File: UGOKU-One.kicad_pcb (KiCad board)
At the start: 2 copper layers, 63 x 63 mm, 57 parts, among them J1 PB0, J2 PA10, J3 Conn_01x02_Male, J4 PA10, J6 Conn_01x04, SW1 PF1, SW2 RESET, SW3 SW_Push_DPDT, SW5 SW_Push_DPDT, T3 PTS_1.5_2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

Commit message: 2024/1/6発注仕様
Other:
- board text added: "UGOKU One Ver0.43 UGOKU Lab 2024-1"
- board text added: "https://github.com/UGOKU-Lab/UGOKU-One"
- board text removed: "UGOKU One Ver0.43 UGOKU-Lab 2024-1"
- board text removed: "https://github.com/UGOKU-Lab/MultiBoardMini_HW"

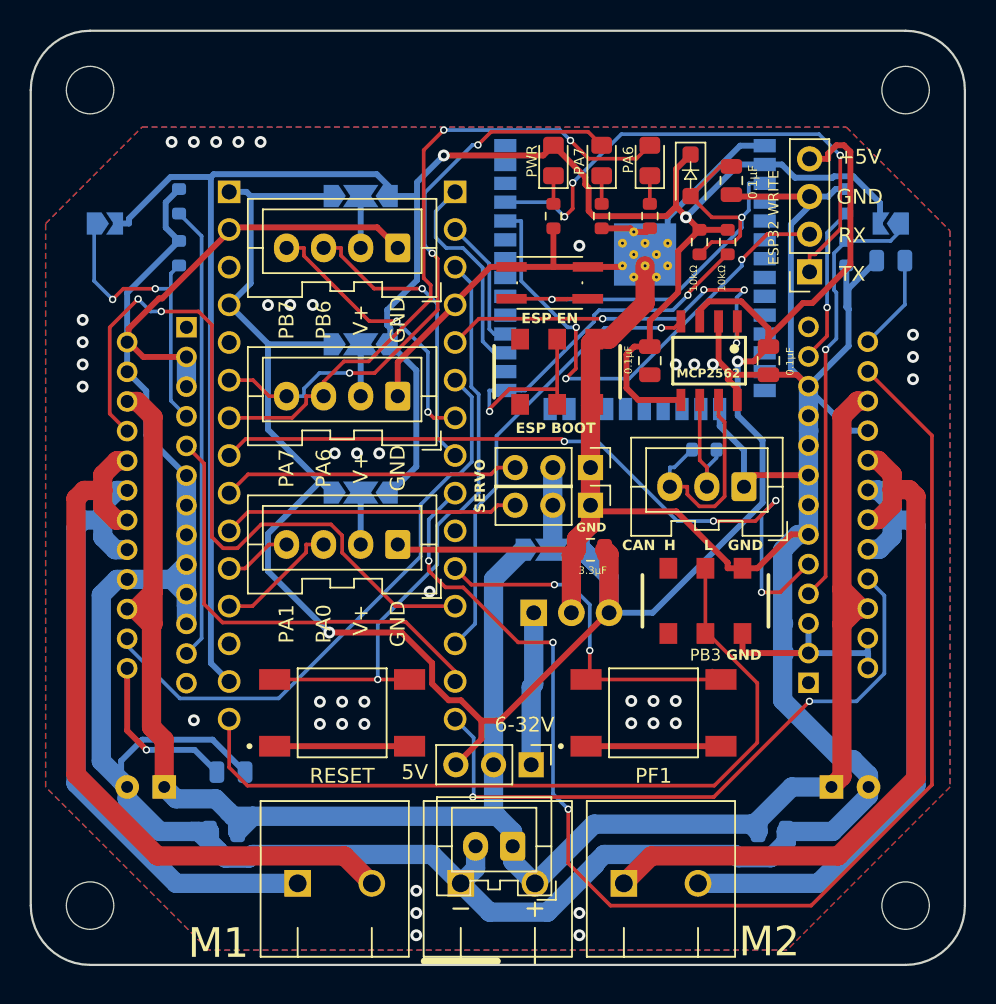
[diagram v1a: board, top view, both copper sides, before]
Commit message: Via size modified to match JLCPCB rules
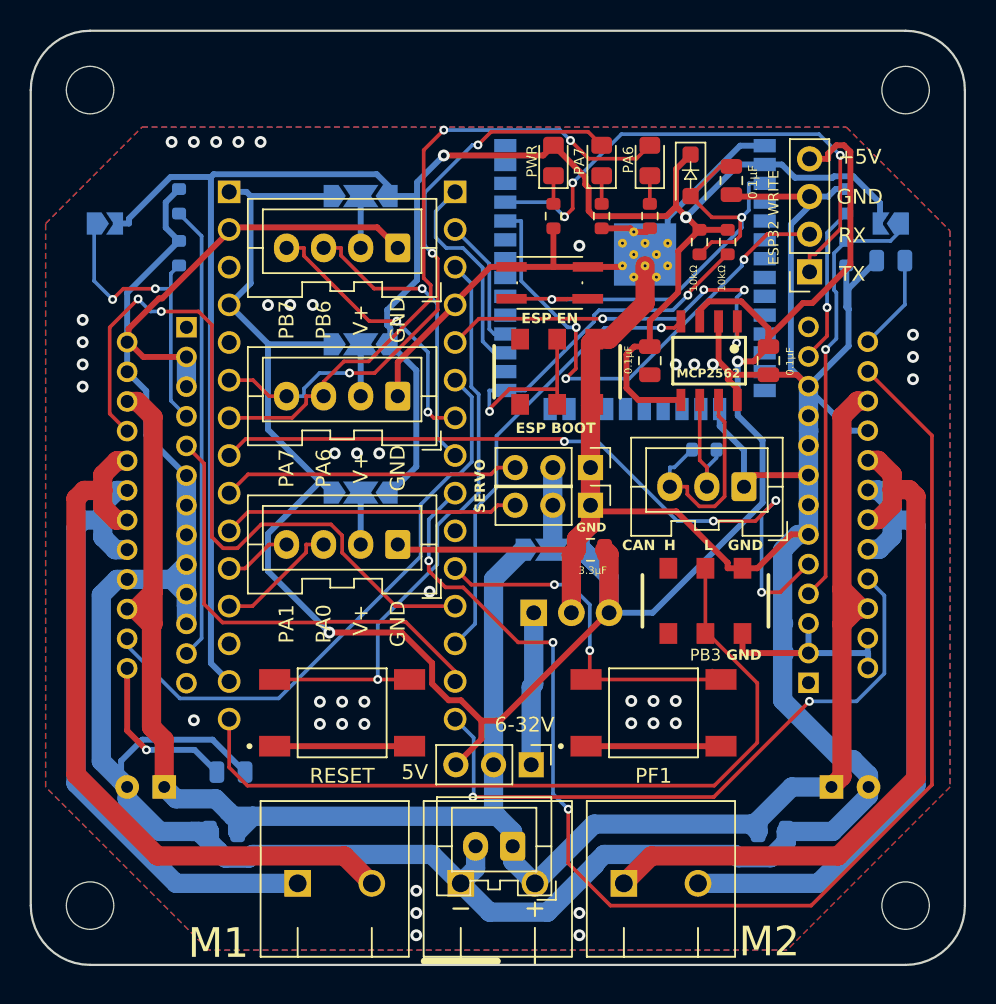
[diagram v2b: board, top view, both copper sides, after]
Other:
- board text added: "UGOKU One Ver0.4.4 UGOKU Lab 2024-1"
- board text removed: "UGOKU One Ver0.43 UGOKU Lab 2024-1"

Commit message: Motor driver STM pin assignment replacement
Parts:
- renumbered MOTOR2 to MOTOR_A1, MOTOR1 to MOTOR_B1
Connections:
- U4 pad 9: Net-(U2B-PA5) -> Net-(U2A-PB5)
- U5 pad 8: Net-(U2A-PA8) -> Net-(U2B-PA5)
- U5 pad 9: Net-(U2A-PB5) -> Net-(U2A-PA8)
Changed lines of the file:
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@@
     (property "Sheetname" "")
     (attr through_hole)
-    (fp_text reference "MOTOR1" (at 0 0) (layer "F.SilkS") hide
+    (fp_text reference "MOTOR_B1" (at 0 0) (layer "F.SilkS") hide
         (effects (font (size 1.27 1.27) (thickness 0.15)) (justify right top))
     )
@@
     (property "Sheetname" "")
     (attr through_hole)
-    (fp_text reference "MOTOR2" (at 0 0) (layer "F.SilkS") hide
+    (fp_text reference "MOTOR_A1" (at 0 0) (layer "F.SilkS") hide
         (effects (font (size 1.27 1.27) (thickness 0.15)) (justify right top))
     )
@@
       (net 32 "Net-(U5-STBY)") (pinfunction "STBY") (pintype "input") (solder_mask_margin 0.102))
     (pad "8" thru_hole circle (at -5 2 270) (size 1.388 1.388) (drill 0.88) (layers "*.Cu" "*.Mask")
-      (net 43 "Net-(U2A-PA8)") (pinfunction "IN1") (pintype "input") (solder_mask_margin 0.102))
+      (net 41 "Net-(U2B-PA5)") (pinfunction "IN1") (pintype "input") (solder_mask_margin 0.102))
     (pad "9" thru_hole circle (at -4 -2 270) (size 1.388 1.388) (drill 0.88) (layers "*.Cu" "*.Mask")
-      (net 22 "Net-(U2A-PB5)") (pinfunction "IN2") (pintype "input") (solder_mask_margin 0.102))
+      (net 43 "Net-(U2A-PA8)") (pinfunction "IN2") (pintype "input") (solder_mask_margin 0.102))
     (pad "10" thru_hole circle (at -3 2 270) (size 1.388 1.388) (drill 0.88) (layers "*.Cu" "*.Mask")
       (net 38 "Net-(U5-OUT2A)") (pinfunction "OUT2B") (pintype "output") (solder_mask_margin 0.102))
@@
       (net 39 "Net-(U2A-PB4)") (pinfunction "IN1") (pintype "input") (solder_mask_margin 0.102))
     (pad "9" thru_hole circle (at -3.97 -2.05 90) (size 1.388 1.388) (drill 0.88) (layers "*.Cu" "*.Mask")
-      (net 41 "Net-(U2B-PA5)") (pinfunction "IN2") (pintype "input") (solder_mask_margin 0.102))
+      (net 22 "Net-(U2A-PB5)") (pinfunction "IN2") (pintype "input") (solder_mask_margin 0.102))
     (pad "10" thru_hole circle (at -2.97 1.95 90) (size 1.388 1.388) (drill 0.88) (layers "*.Cu" "*.Mask")
       (net 36 "Net-(U4-OUT2A)") (pinfunction "OUT2B") (pintype "output") (solder_mask_margin 0.102))

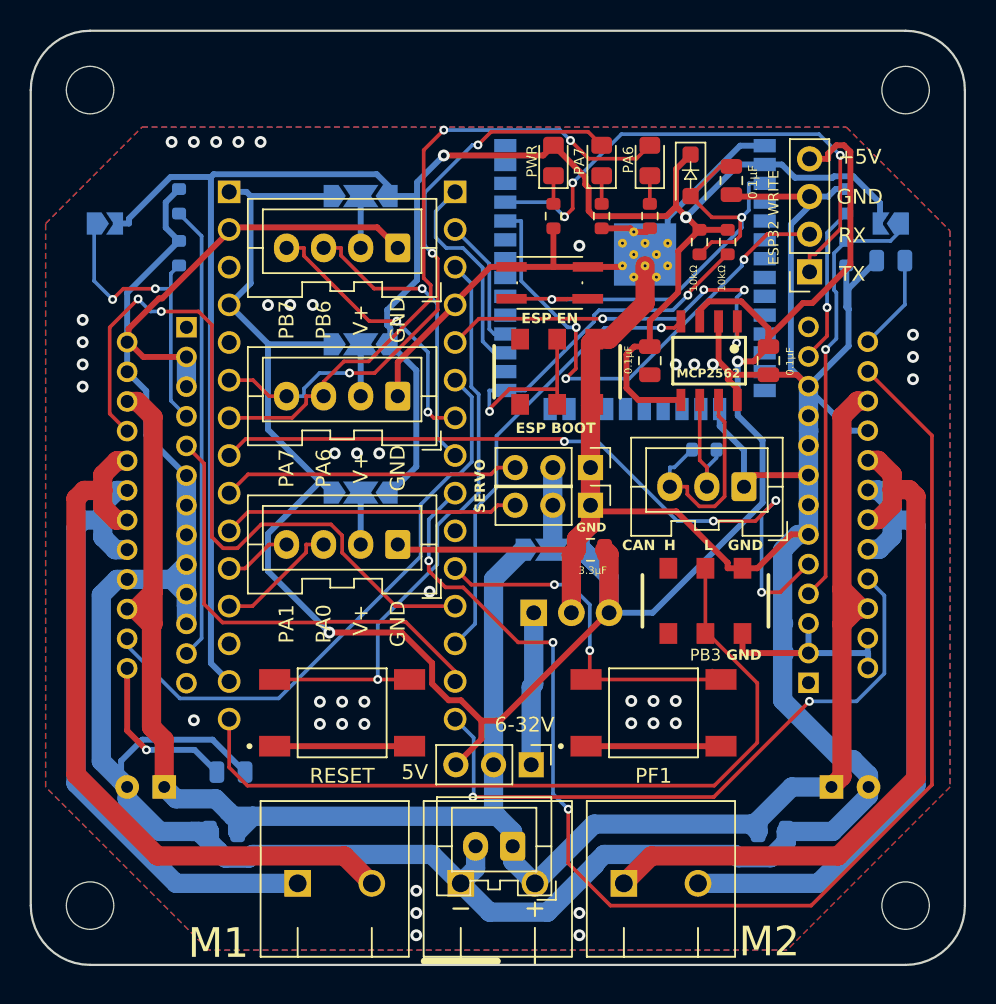
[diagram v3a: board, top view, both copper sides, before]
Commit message: Motor driver STM pin assignment replacement completed
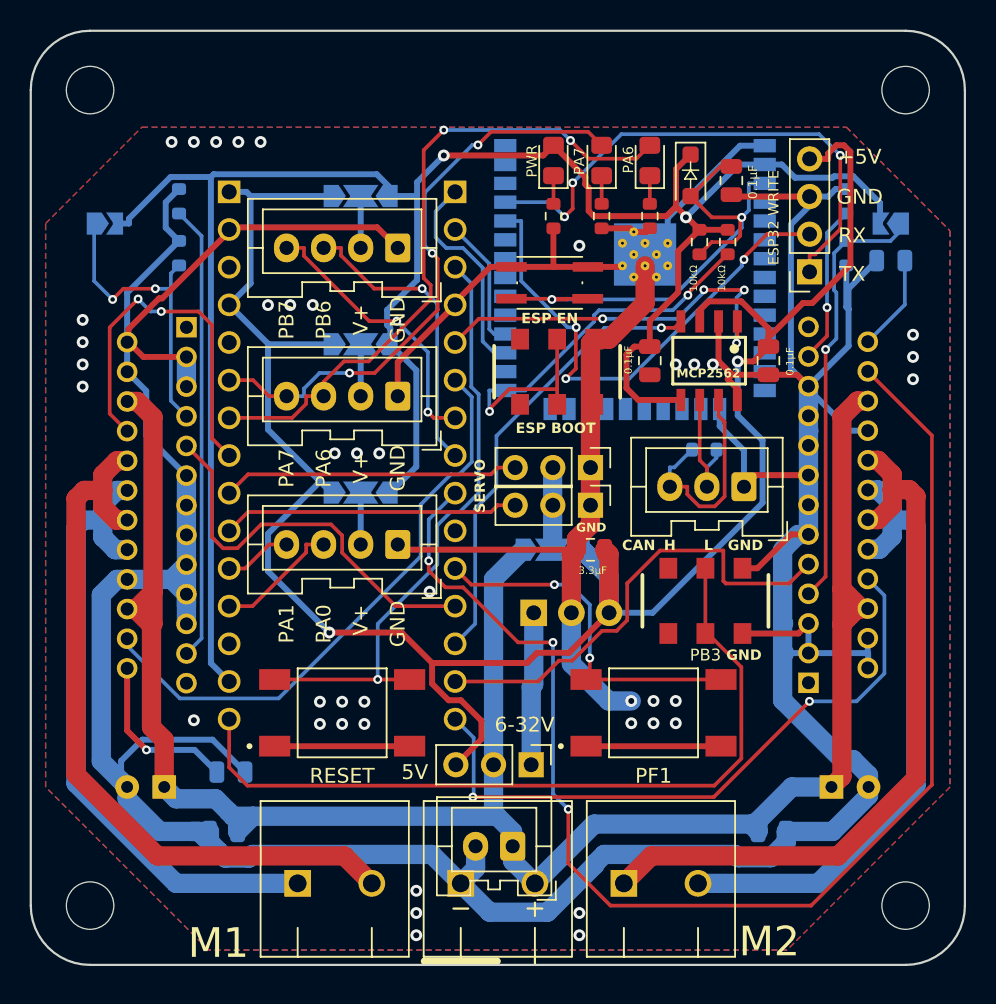
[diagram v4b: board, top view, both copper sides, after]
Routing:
- net Net-(U2B-PA5): track 50.7 -> 25.2 mm, vias 4 -> 2
- net Net-(U2A-PA8): track 50.5 -> 27.2 mm, vias 2 -> 0
- net GND: track 395.1 -> 390.6 mm
- net +5V: track 140.1 -> 141.8 mm
- net Net-(U2A-PB5): track 30.7 -> 31.6 mm
- net Net-(U2B-PB3): track 53.9 -> 53.0 mm

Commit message: update silk version
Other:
- board text added: "UGOKU One Ver0.4.4 UGOKU Lab 2024-2"
- board text removed: "UGOKU One Ver0.4.4 UGOKU Lab 2024-1"
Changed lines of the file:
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@@
     (effects (font (size 1.1 1.1) (thickness 0.18)) (justify mirror))
   )
-  (gr_text "UGOKU One Ver0.4.4 UGOKU Lab 2024-1" (at 30.3 0 90) (layer "B.SilkS")
+  (gr_text "UGOKU One Ver0.4.4 UGOKU Lab 2024-2" (at 30.3 0 90) (layer "B.SilkS")
     (effects (font (size 1 1) (thickness 0.15)) (justify mirror))
   )

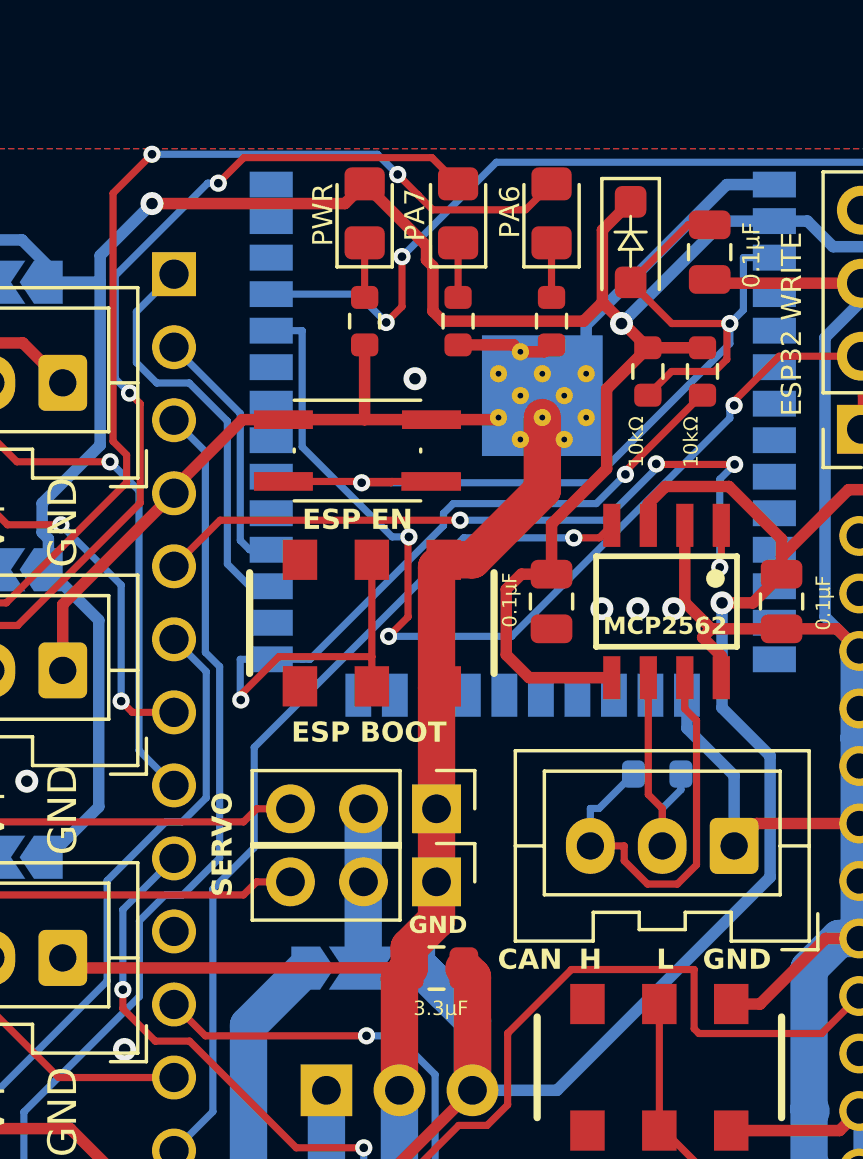
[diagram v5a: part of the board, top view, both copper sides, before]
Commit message: Update Diode footprint and servo pin header
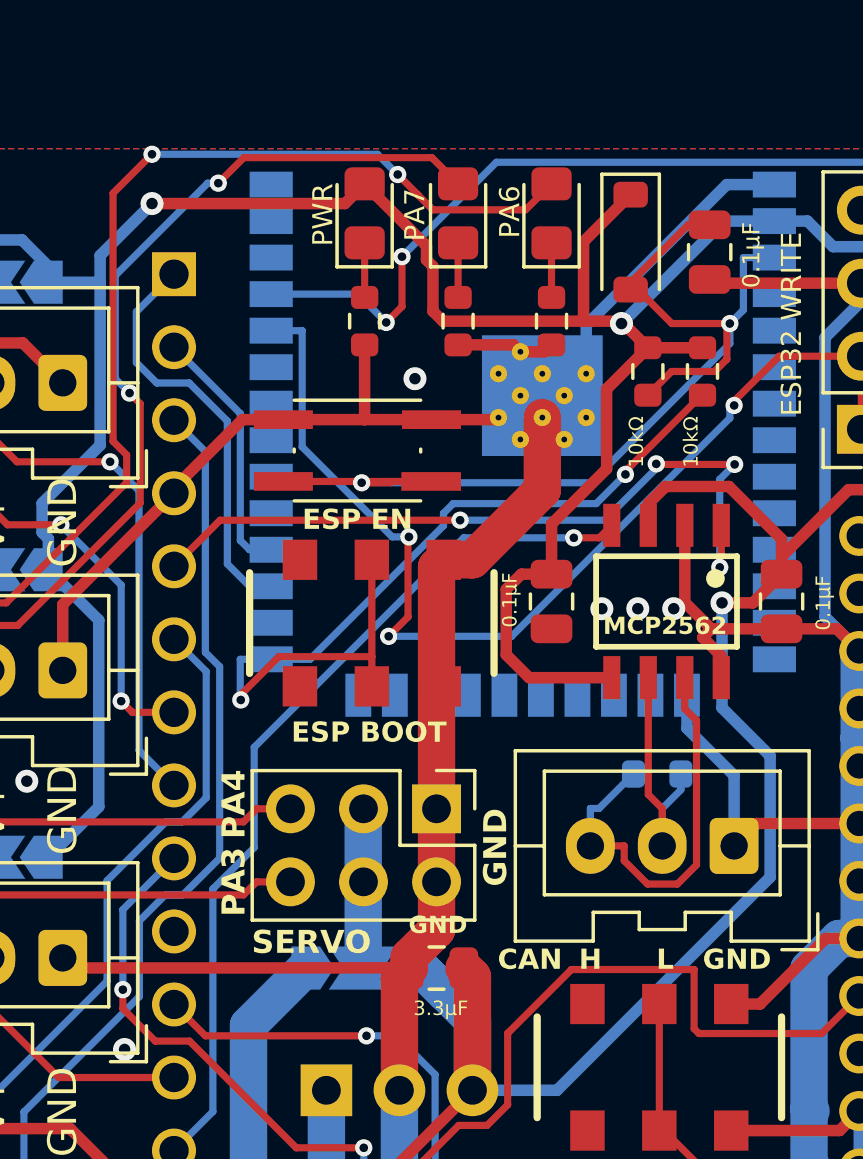
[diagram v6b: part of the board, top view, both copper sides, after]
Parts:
- removed J1: PB0, Connector_PinHeader_2.54mm:PinHeader_1x03_P2.54mm_Vertical
- D1: footprint Diode_SMD:D_SOD-123F -> Diode_SMD:D_SOD-123
- J2: value PA10 -> Conn_02x03_Odd_Even; footprint Connector_PinHeader_2.54mm:PinHeader_1x03_P2.54mm_Vertical -> Connector_PinHeader_2.54mm:PinHeader_2x03_P2.54mm_Vertical
- moved J2 2.54 mm to (6.25, -2.04)
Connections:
- J2 pad 2: Net-(J1-Pin_2) -> GND
- JP4 pad 2: Net-(J1-Pin_2) -> Net-(J2-Pin_3)
- U2 pad 4_10: Net-(J2-Pin_3) -> Net-(J2-Pin_6)
- U2 pad 4_9: Net-(J1-Pin_3) -> Net-(J2-Pin_5)
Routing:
- net Net-(J2-Pin_6): track 0.00 -> 20.0 mm
- net Net-(J2-Pin_5): track 0.00 -> 20.0 mm
- net Net-(J1-Pin_3): track 20.0 -> 0.00 mm
- net Net-(J2-Pin_3): track 20.0 -> 5.79 mm
- net Net-(J1-Pin_2): track 5.79 -> 0.00 mm
- net +3V3: track 145.2 -> 145.8 mm
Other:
- board text added: "PA3"
- board text added: "PA4"

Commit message: XA使用Verの最終版
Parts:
- renumbered IO_3 to CN1, ENC/IO_2 to CN2, ENC/IO_1 to CN3, CAN1 to CN4, MOTOR_A1 to T1, MOTOR_B1 to T2

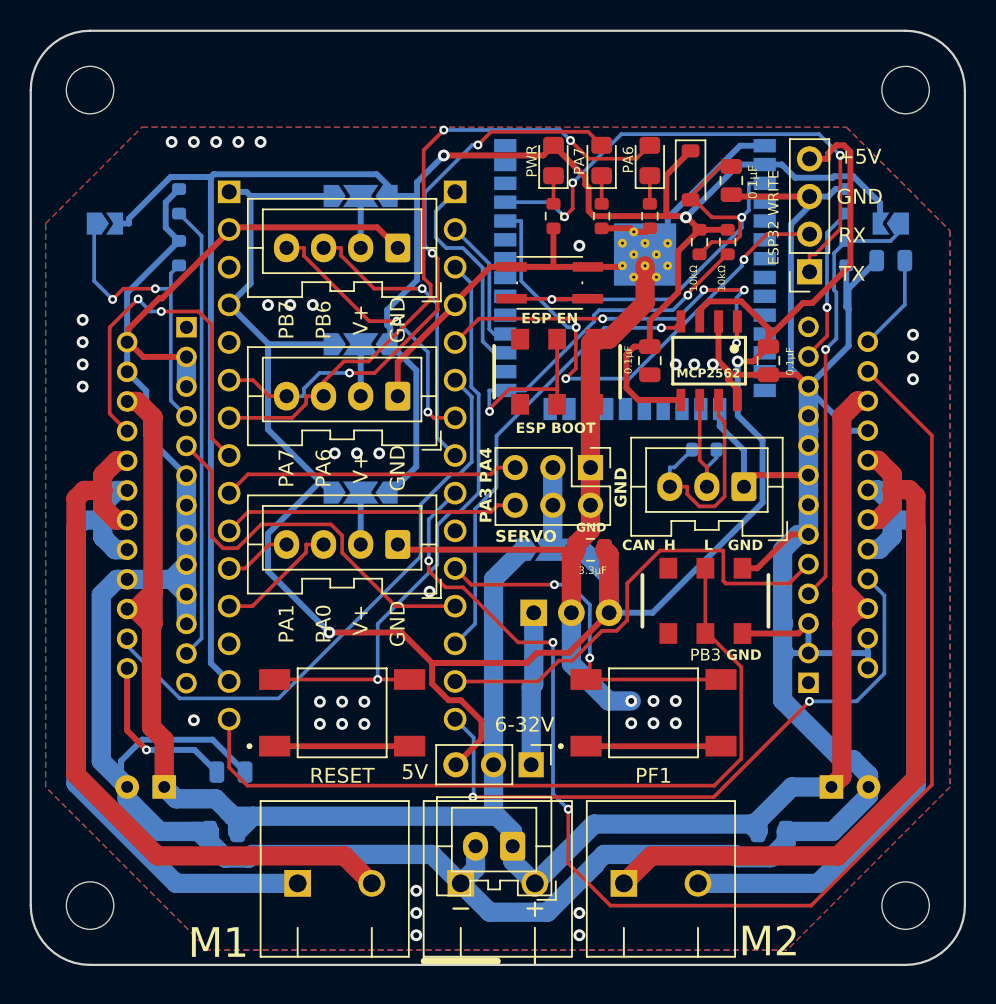
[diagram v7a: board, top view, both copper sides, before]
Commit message: IOコネクタを圧着不要コネクタhar-flexicon化する検討を開始
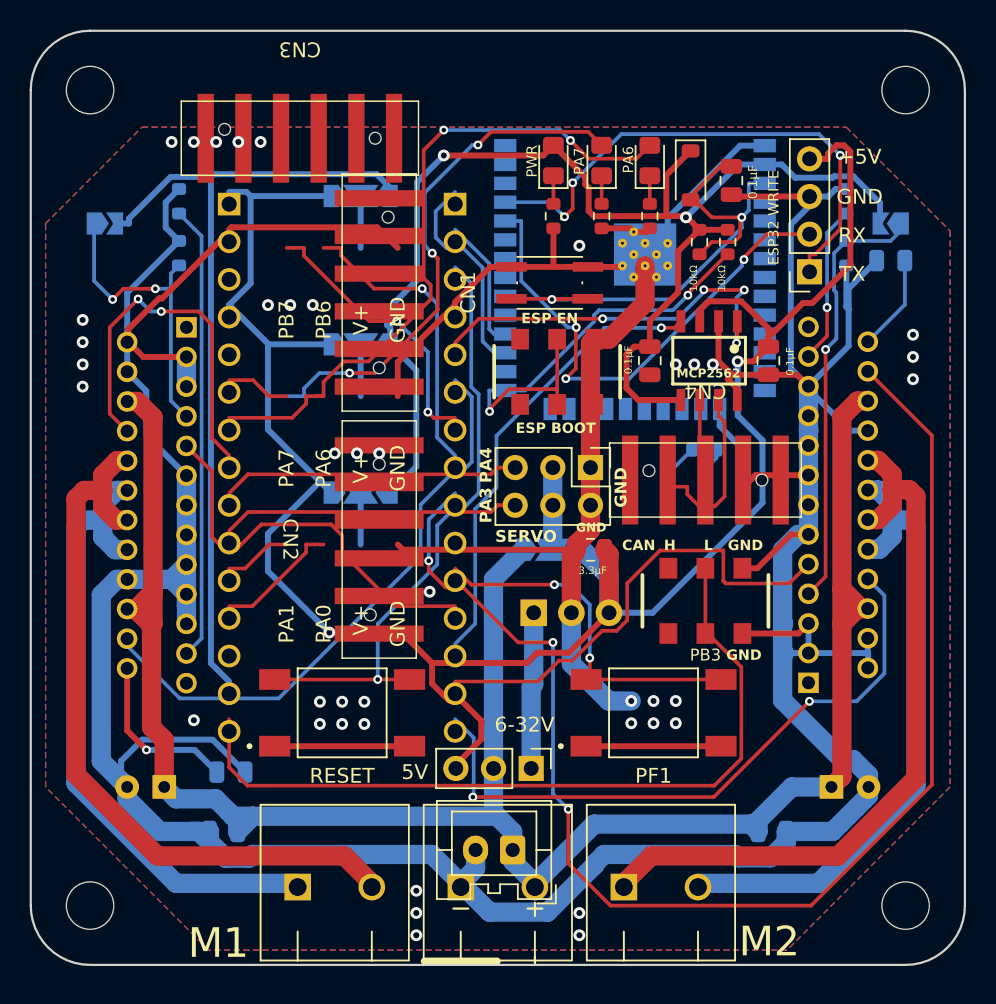
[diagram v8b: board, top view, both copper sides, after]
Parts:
- CN1, CN2, CN3: footprint Connector_JST:JST_XA_B04B-XASK-1_1x04_P2.50mm_Vertical -> UGOKU-One_Libraries:har-flexicon_2.54_4pin
- CN4: footprint Connector_JST:JST_XA_B03B-XASK-1_1x03_P2.50mm_Vertical -> UGOKU-One_Libraries:har-flexicon_2.54_3pin
- moved CN3 27.5 mm to (-13.3, -24.2)
- moved CN2 9.98 mm to (-8.00, 2.81), turned to -90 degrees
- moved CN1 3.91 mm to (-8.00, -13.8), turned to 90 degrees
- moved CN4 2.64 mm to (14.0, -1.20)
- moved U2 0.83 mm to (-10.5, -2.03)
- moved J3 0.25 mm to (1.00, 23.8)
- moved J4 0.25 mm to (2.25, 18.2)
- moved T1 0.25 mm to (-11.0, 26.2)
- moved T2 0.25 mm to (11.0, 26.2)
- moved T3 0.25 mm to (0.00, 26.2)
